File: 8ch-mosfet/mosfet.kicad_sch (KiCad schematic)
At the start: 18 parts, among them J5 Screw_Terminal_01x02, Q1 IPB110P06LM, Q2 2N7002, Q21 BC846, Q22 BC856, U5 ACS725xLCTR-20AU

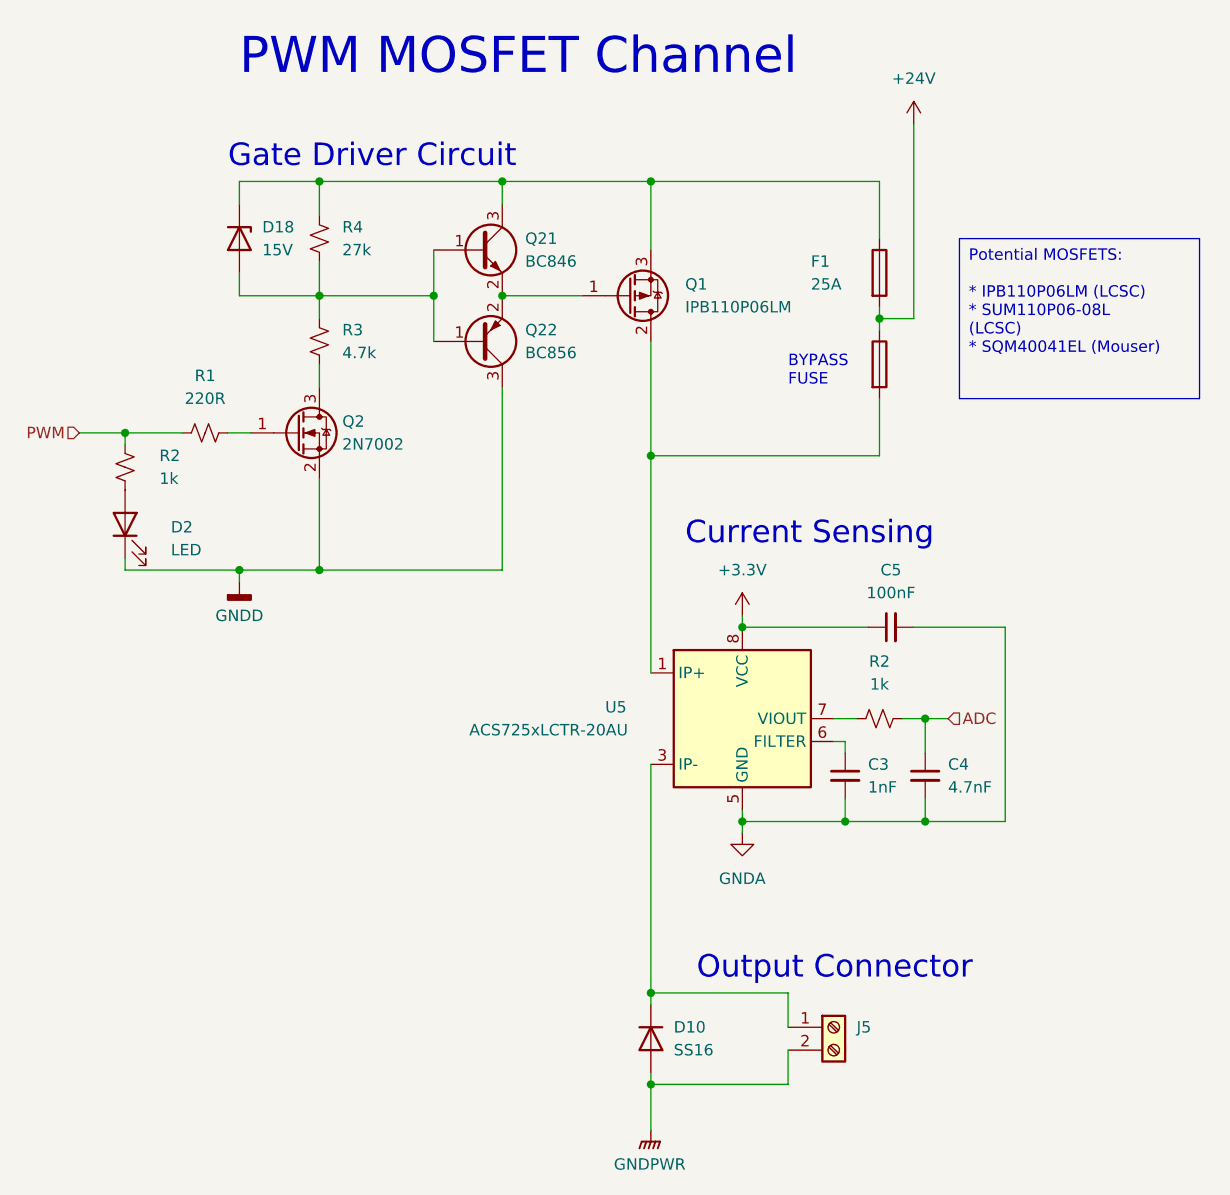
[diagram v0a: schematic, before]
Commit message: changed to MCP3564
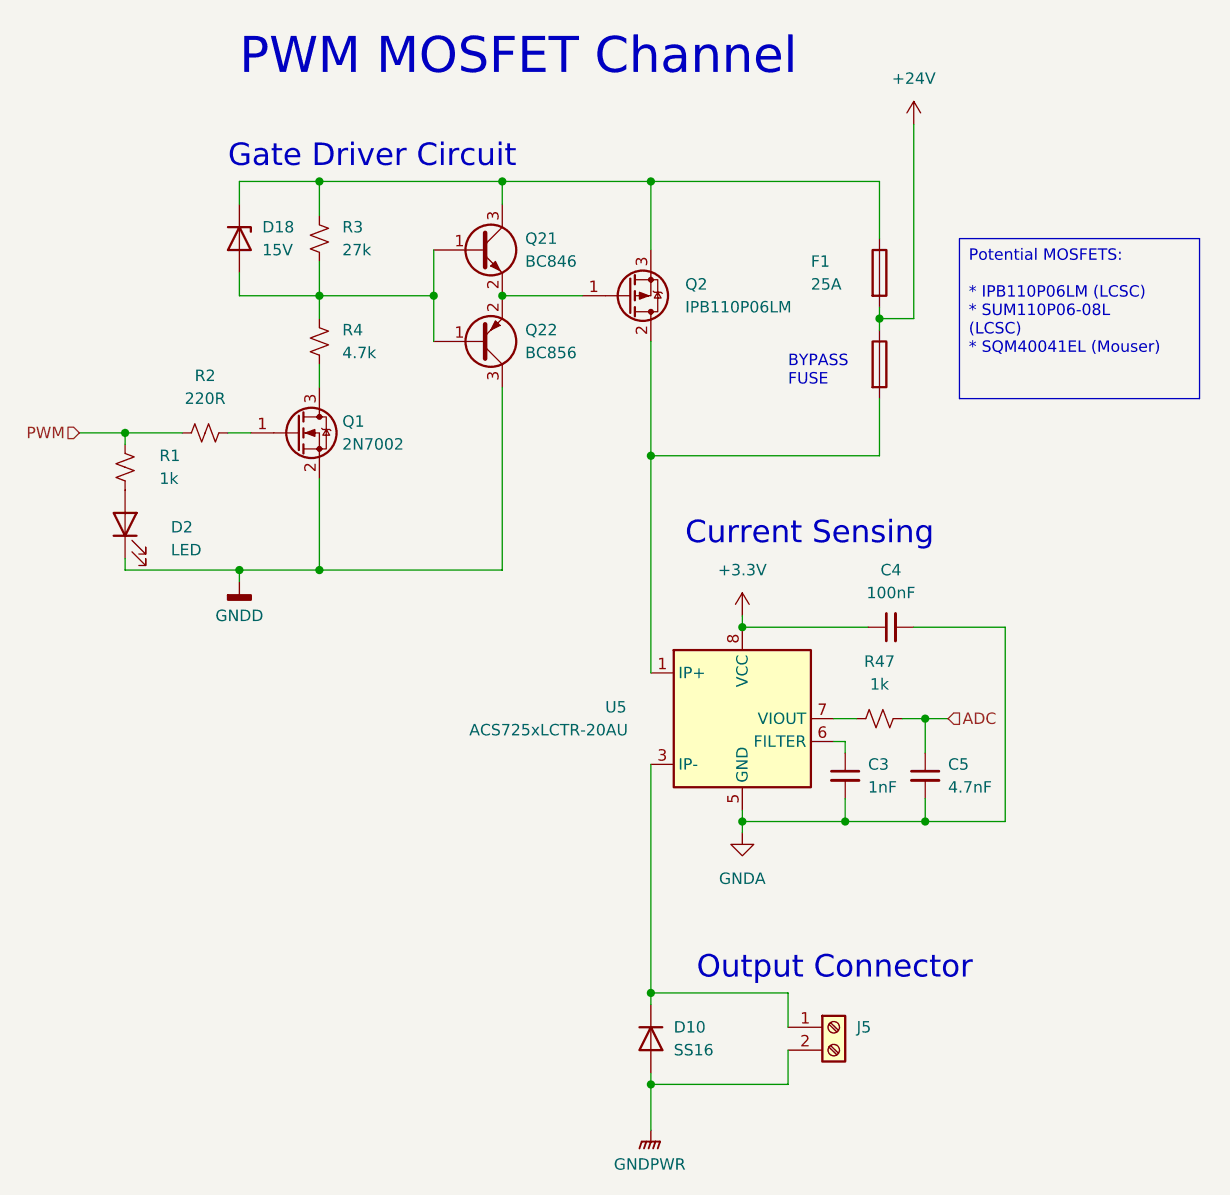
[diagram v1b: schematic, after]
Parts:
- renumbered C5 to C4, C4 to C5, Q2 to Q1, Q1 to Q2, R2 to R1, R1 to R2, R4 to R3, R3 to R4, R2 to R47

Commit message: more progress on new 8ch board.
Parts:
- removed J5: Screw_Terminal_01x02, yarrboard:Molex 1x02 .375, symbol Connector:Screw_Terminal_01x02
- added J1: Conn_01x01, yarrboard:T44001, symbol Connector_Generic:Conn_01x01
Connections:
- net at D10.1 (K), U5.3 (IP-), U5.4 (IP-): now also F1.3, J1.1 (Pin_1)
- net at Q2.2 (D), U5.1 (IP+), U5.2 (IP+): no longer F1.3
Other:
- note removed: "Output Connector"

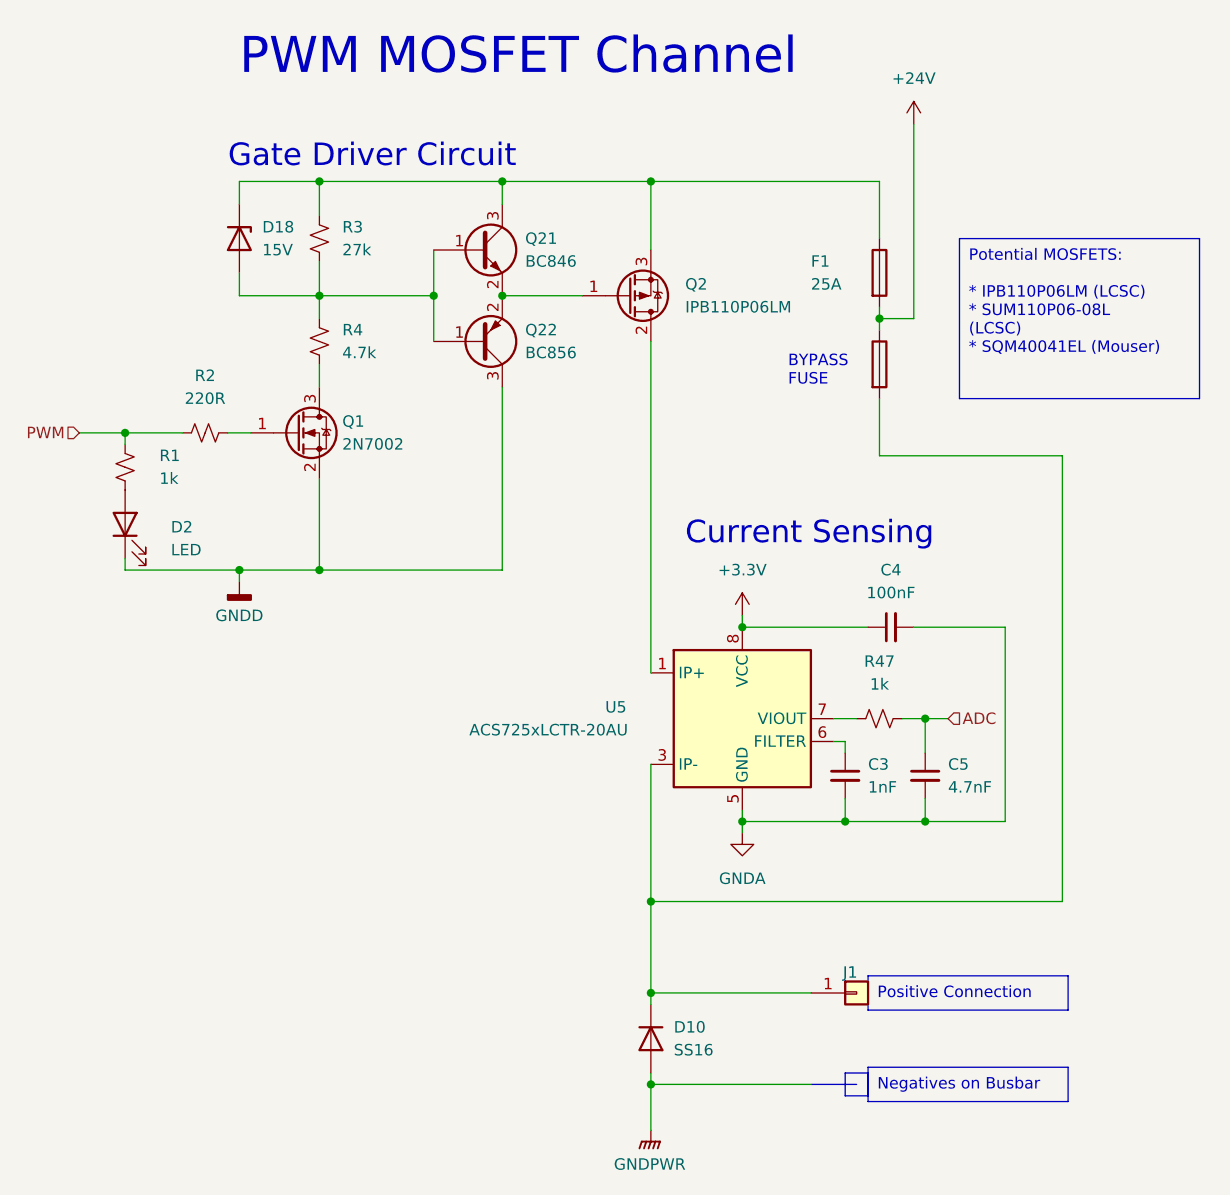
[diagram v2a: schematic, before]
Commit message: big update - 12ch, volt adc, senders, etc.
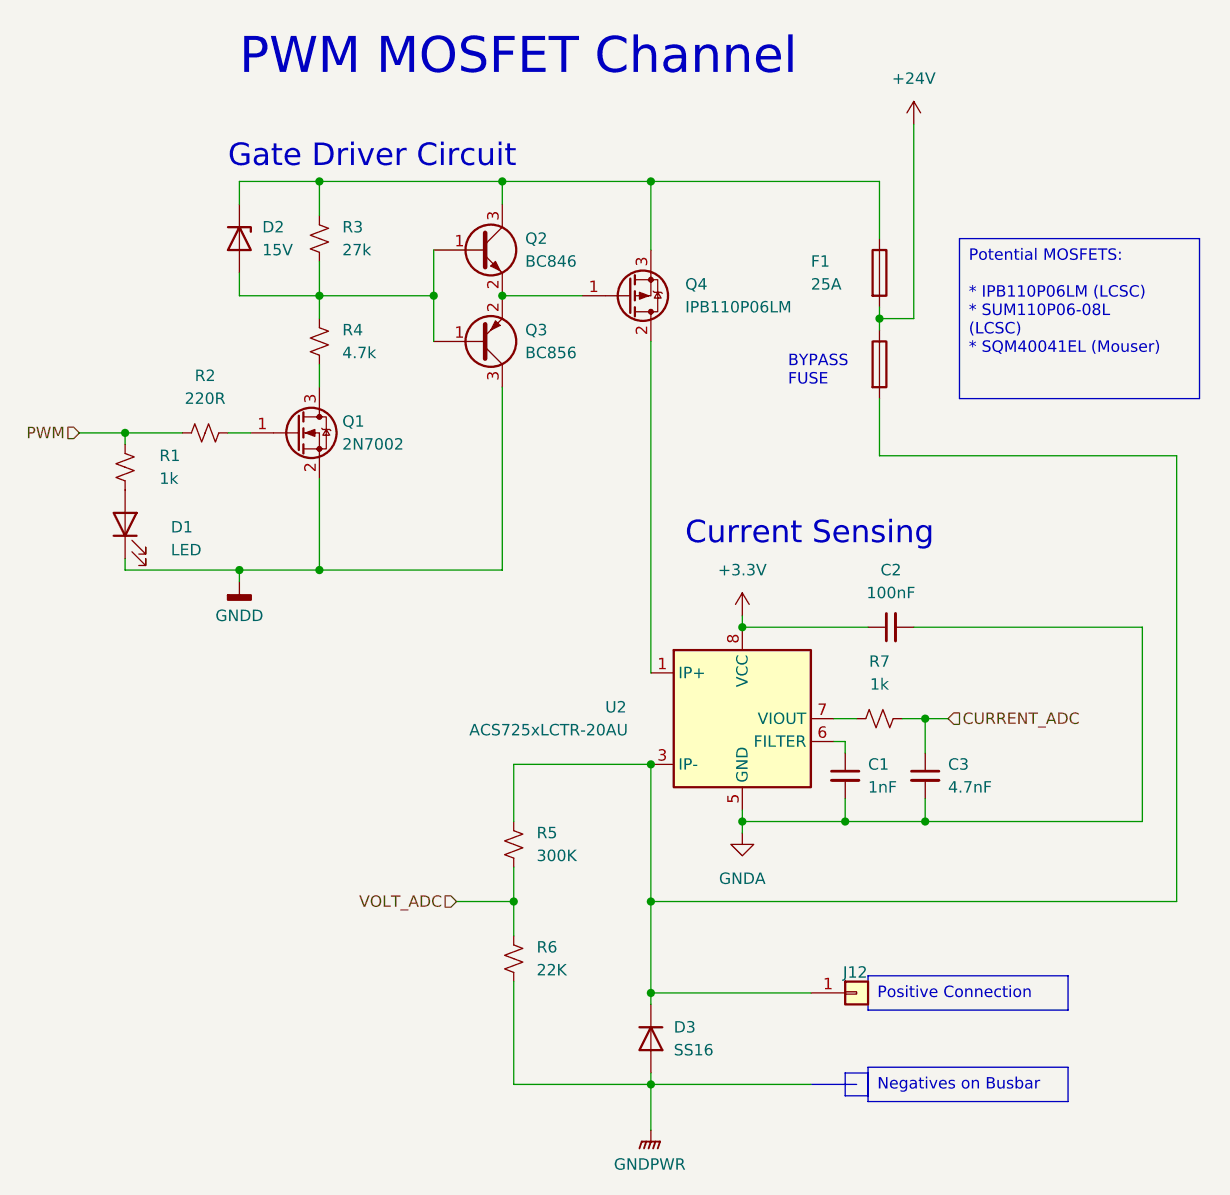
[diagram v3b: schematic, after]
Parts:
- added R5: 300K, Resistor_SMD:R_0805_2012Metric_Pad1.20x1.40mm_HandSolder, symbol Device:R_Small_US
- added R6: 22K, Resistor_SMD:R_0805_2012Metric_Pad1.20x1.40mm_HandSolder, symbol Device:R_Small_US
- renumbered C3 to C1, C4 to C2, C5 to C3, D2 to D1, D18 to D2, D10 to D3, J1 to J12, Q21 to Q2, Q22 to Q3, Q2 to Q4, R47 to R7, U5 to U2
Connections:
- net GNDPWR: now also R6.1
- net at D3.1 (K), F1.3, J12.1 (Pin_1)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: now also R5.2
- net ADC renamed CURRENT_ADC
- new net VOLT_ADC: R5.1, R6.2

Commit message: component layout looking crispy.
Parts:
- renumbered J12 to J1, R1 to R3, R2 to R4, R3 to R5, R4 to R6, R5 to R7, R6 to R8, R7 to R9
